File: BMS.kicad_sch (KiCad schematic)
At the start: 10 parts, among them Q1 DMN3025LFG, Q2 DMN3025LFG, U1 S-82A2AAA-I8T1U7

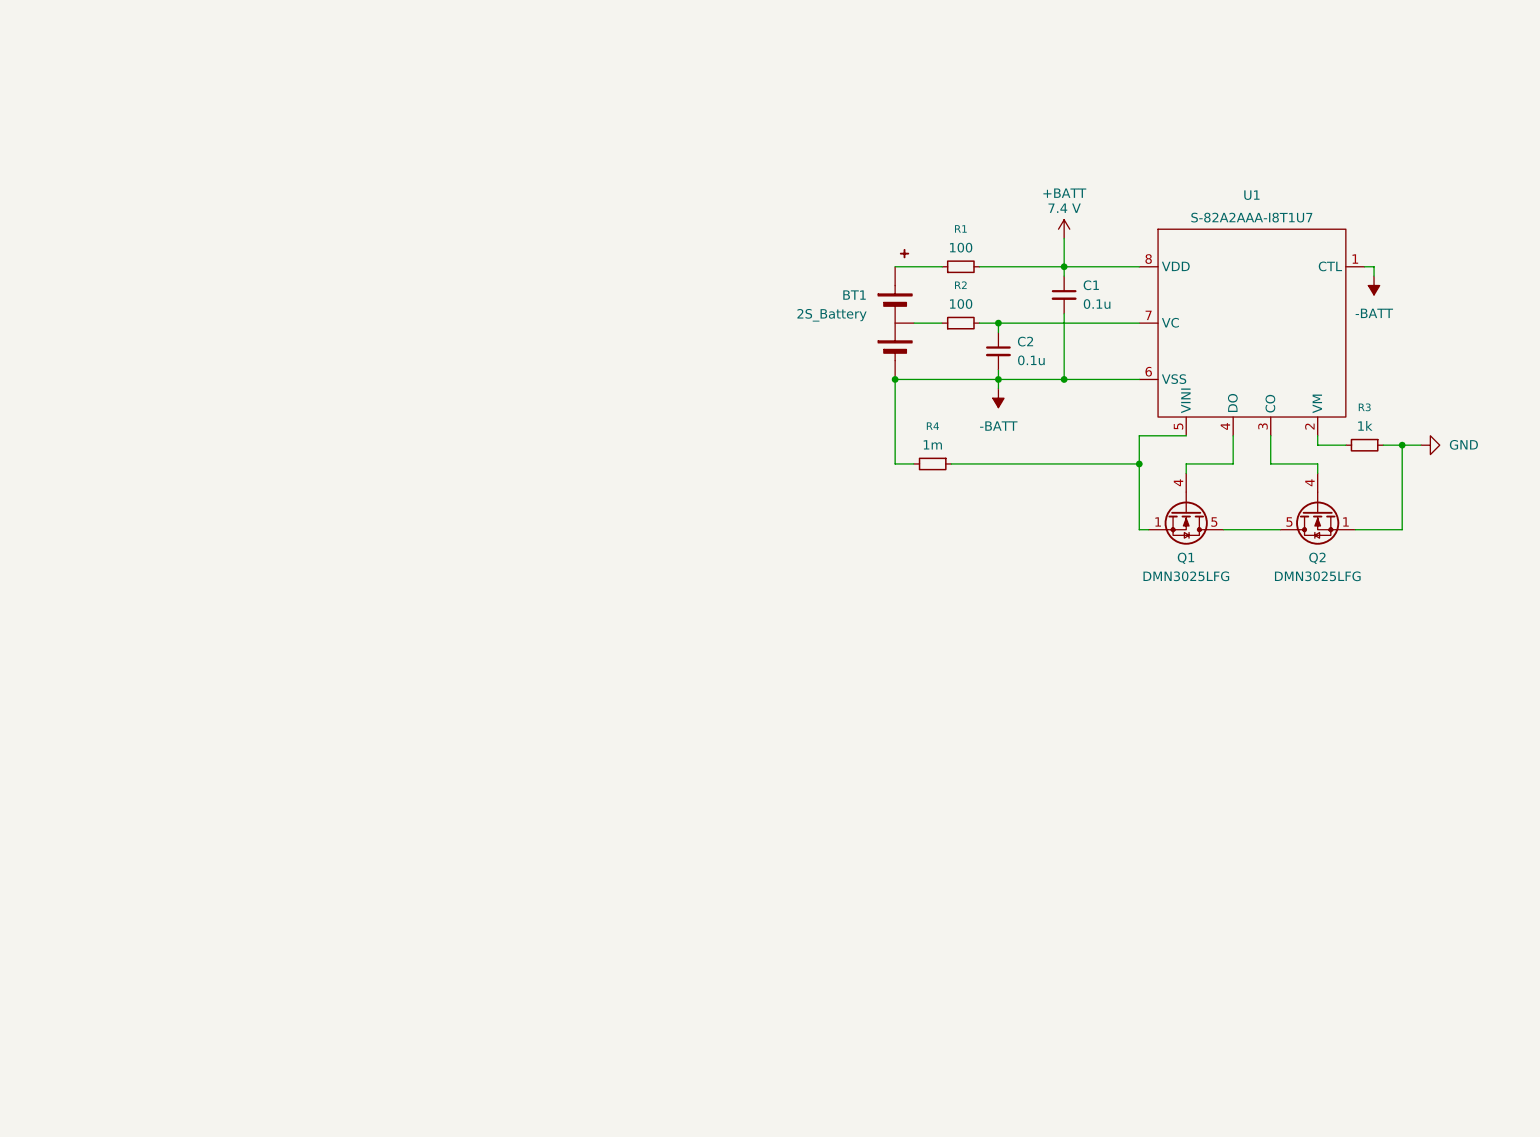
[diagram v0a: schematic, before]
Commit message: Finalized charger detection circuit, designed voltage monitor circuit, added pogo connector, finalized motor driver connections, added ESP32 connections
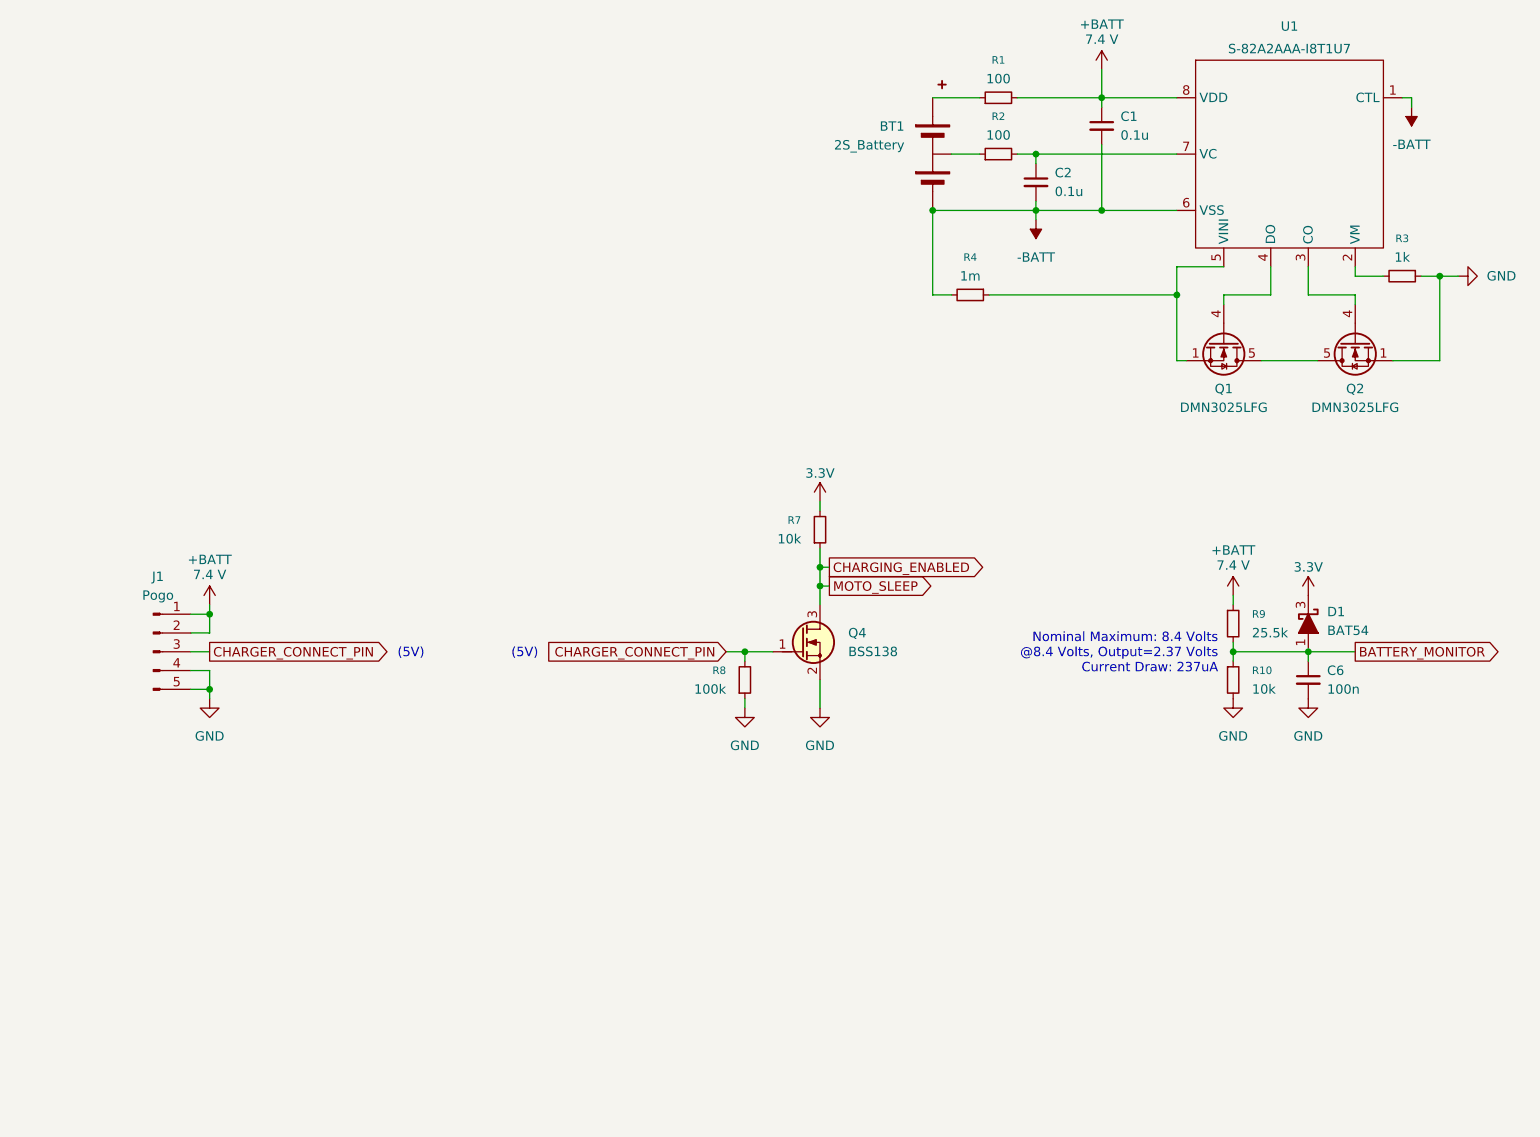
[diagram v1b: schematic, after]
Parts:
- added C6: 100n, symbol Device:C_Small
- added D1: BAT54, PCM_Package_TO_SOT_SMD_AKL:SOT-23, symbol PCM_Diode_Schottky_AKL:BAT54
- added J1: Pogo, symbol Connector:Conn_01x05_Pin
- added Q4: BSS138, PCM_Package_TO_SOT_SMD_AKL:SOT-23, symbol PCM_Transistor_MOSFET_AKL:BSS138
- added R10, R7: 10k, symbol Device:R_Small
- added R8: 100k, symbol Device:R_Small
- added R9: 25.5k, symbol Device:R_Small
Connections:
- net +BATT: now also J1.1 (Pin_1), J1.2 (Pin_2), R9.1
- net GND: now also C6.2, J1.4 (Pin_4), J1.5 (Pin_5), Q4.2 (S), R10.2, R8.1
- new net 3.3V: D1.3 (K), R7.2
- new net BATTERY_MONITOR: C6.1, D1.1 (A), R10.1, R9.2
- new net CHARGER_CONNECT_PIN: J1.3 (Pin_3), Q4.1 (G), R8.2
- new net CHARGING_ENABLED: Q4.3 (D), R7.1
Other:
- note added: "(5V)"
- note added: "Nominal Maximum: 8.4 Volts @8.4 Volts, Output=2.37 Volts Current Draw: 237uA"
- moved on the sheet: BT1, C1, C2, Q1, Q2, R1, R2, R3, R4, U1

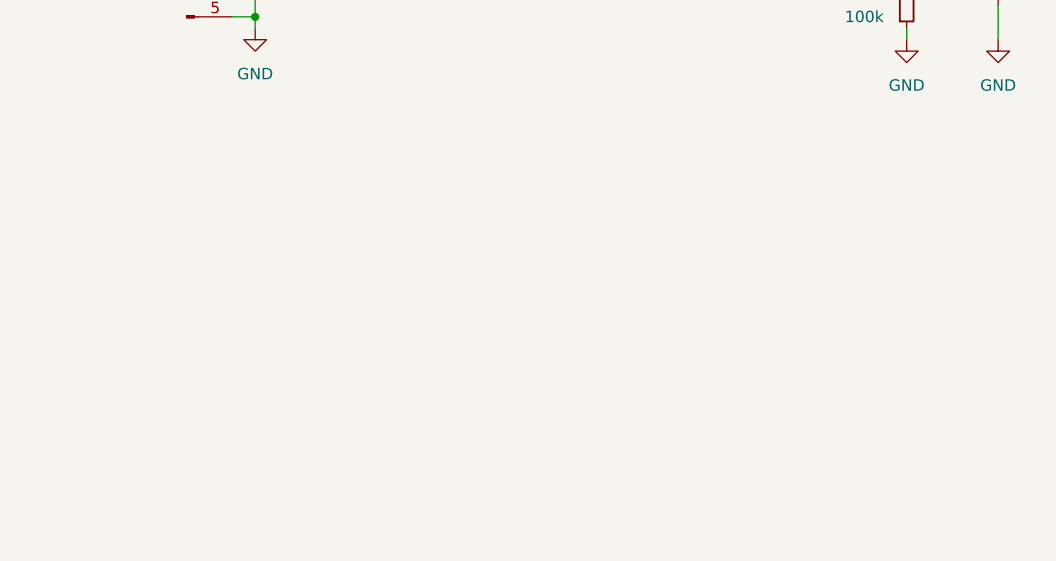
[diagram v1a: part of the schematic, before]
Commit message: Assigned footprints, new pogo footprint, added test points
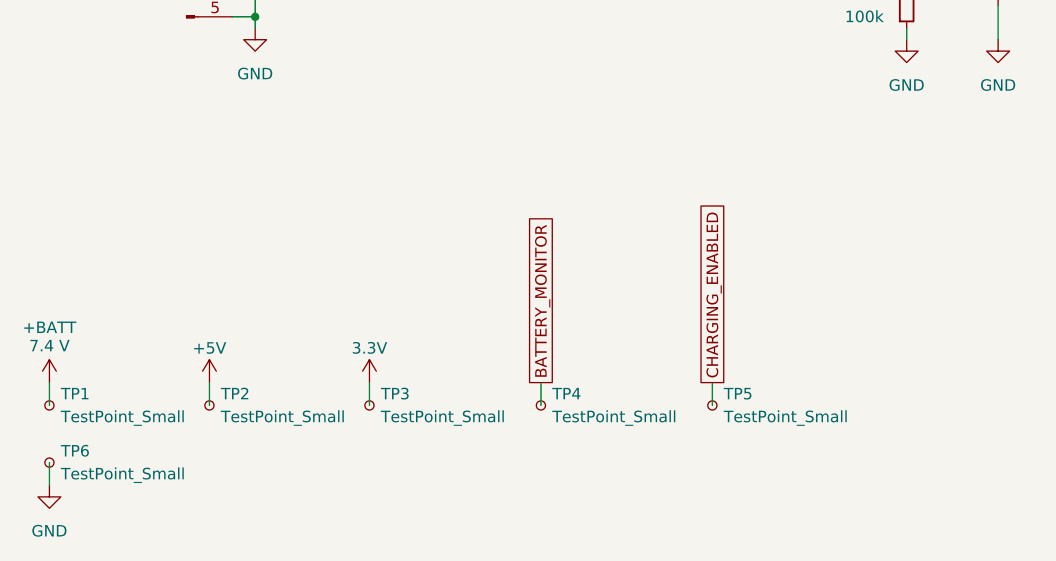
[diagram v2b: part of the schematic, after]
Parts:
- added TP1, TP2, TP3, TP4, TP5, TP6: TestPoint_Small, TestPoint:TestPoint_Pad_D1.0mm, symbol Connector:TestPoint_Small
- C1, C2, C6: footprint (none) -> Capacitor_SMD:C_1206_3216Metric_Pad1.33x1.80mm_HandSolder
- J1: footprint (none) -> Pogo:Pogo_Connector_5
- R1, R10, R2, R3, R4, R7, R8, R9: footprint (none) -> Resistor_SMD:R_1206_3216Metric_Pad1.30x1.75mm_HandSolder
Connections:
- net +BATT: now also TP1.1
- net 3.3V: now also TP3.1
- net BATTERY_MONITOR: now also TP4.1
- net CHARGING_ENABLED: now also TP5.1
- net GND: now also TP6.1
- new net +5V: TP2.1
